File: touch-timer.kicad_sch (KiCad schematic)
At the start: 26 parts, among them Q1 Q_PMOS_GDS, Q2 2N3904, SW1 SW_Push, U1 WeMos_D1_mini

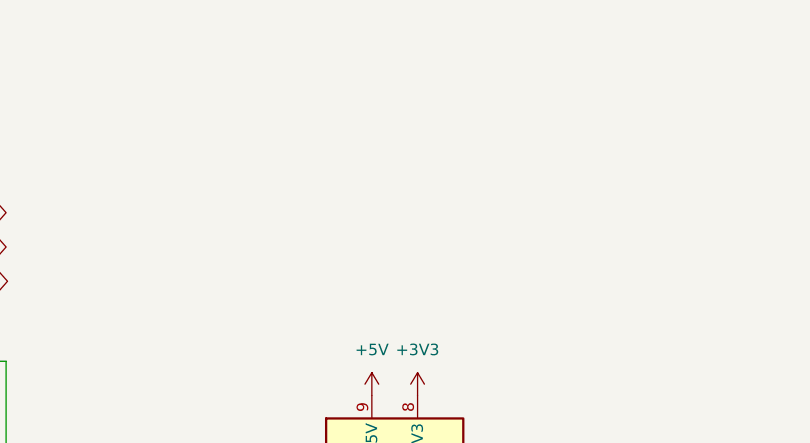
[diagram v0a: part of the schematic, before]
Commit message: Add Lolin C3 and place the leds in a circular fashion
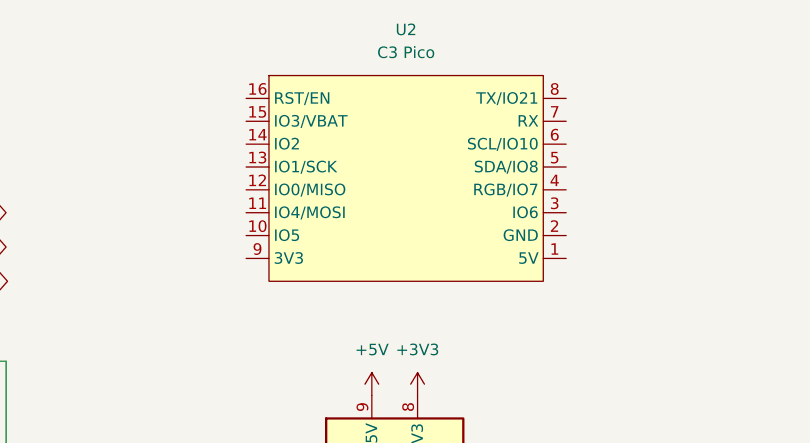
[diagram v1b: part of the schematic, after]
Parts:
- added U2: C3 Pico, c3-pico:c3-pico, symbol c3-pico:c3-pico
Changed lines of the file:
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@@
+    )
+  )
+  (symbol (lib_id "c3-pico:c3-pico") (at 220.98 31.75 0) (unit 1)
+    (in_bom yes) (on_board yes) (dnp no) (fields_autoplaced)
+    (property "Reference" "U2" (at 220.98 15.24 0)
+      (effects (font (size 1.27 1.27)))
+    )
+    (property "Value" "C3 Pico" (at 220.98 17.78 0)
+      (effects (font (size 1.27 1.27)))
+    )
+    (property "Footprint" "c3-pico:c3-pico" (at 220.98 44.45 0)
+      (effects (font (size 1.27 1.27)) hide)
+    )
+    (property "Datasheet" "https://www.wemos.cc/en/latest/c3/c3_pico.html" (at 224.79 46.99 0)
+      (effects (font (size 1.27 1.27)) hide)
+    )
+    (pin "16")
+    (pin "6")
+    (pin "5")
+    (pin "9")
+    (pin "4")
+    (pin "8")
+    (pin "2")
+    (pin "13")
+    (pin "7")
+    (pin "14")
+    (pin "12")
+    (pin "11")
+    (pin "1")
+    (pin "10")
+    (pin "15")
+    (pin "3")
+    (instances
+      (project "touch-timer"
+        (path "/f9ef1ca8-8797-45a6-b22d-0438aff1e5f8"
+          (reference "U2") (unit 1)
+        )
+      )
     )
   )
